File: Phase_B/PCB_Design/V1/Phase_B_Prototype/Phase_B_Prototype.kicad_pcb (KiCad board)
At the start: 2 copper layers, 27 parts, among them J1 USB_B_Mini, U1 CA56-12EWA, U2 74HC595, U3 ATmega32U4-A, Y1 Crystal_GND24

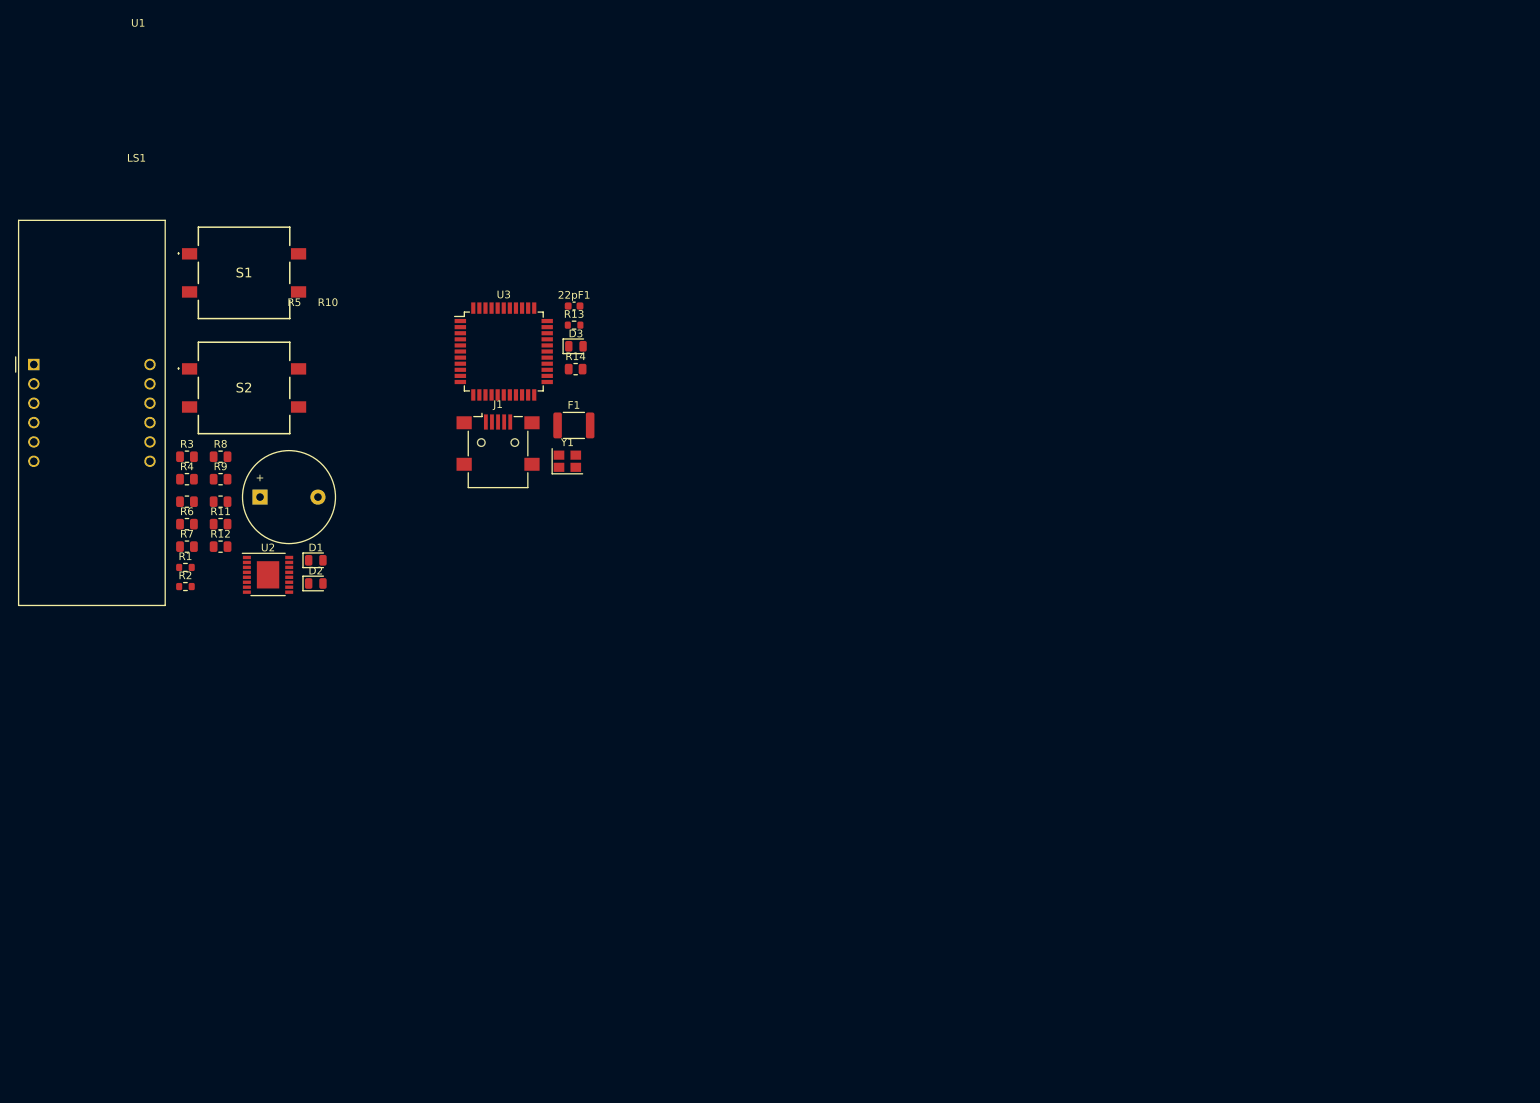
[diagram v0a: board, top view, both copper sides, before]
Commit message: Phase B has received a template. Phase A unchanged.
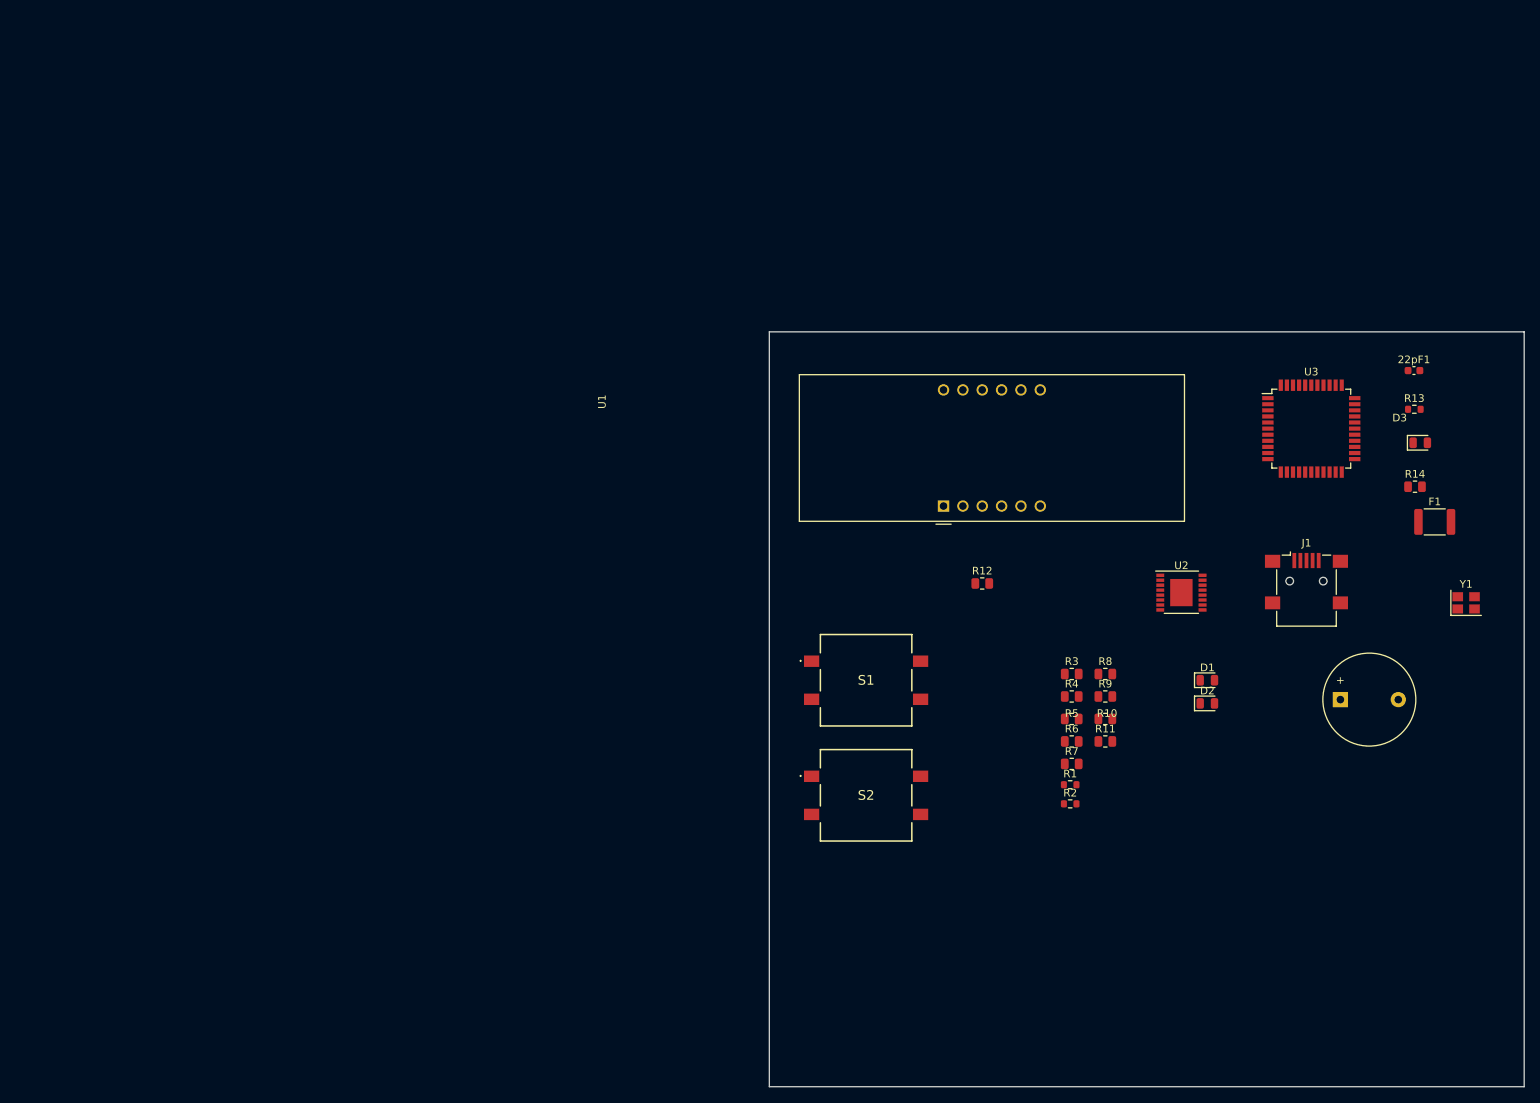
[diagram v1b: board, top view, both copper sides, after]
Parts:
- moved LS1 144.2 mm to (207.0, 101.6)
- moved U1 120.8 mm to (154.9, 76.2), turned to 90 degrees
- moved U2 119.9 mm to (186.2, 87.6)
- moved R10 119.6 mm to (176.2, 104.1)
- moved R11 119.6 mm to (176.2, 107.1)
- moved R8 119.6 mm to (176.2, 98.2)
- moved R9 119.6 mm to (176.2, 101.2)
- moved R1 119.6 mm to (171.6, 112.8)
- moved R2 119.6 mm to (171.6, 115.3)
- moved R3 119.6 mm to (171.8, 98.2)
- moved R4 119.6 mm to (171.8, 101.2)
- moved R5 119.6 mm to (171.8, 104.1)
- moved R6 119.6 mm to (171.8, 107.1)
- moved R7 119.6 mm to (171.8, 110.0)
- moved Y1 119.4 mm to (223.5, 88.9)
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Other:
- board outline added: 99.1 x 99.1 mm
